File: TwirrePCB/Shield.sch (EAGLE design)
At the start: 60 parts, among them Q1 BSS138, Q2 BSS138, T3 FMMT591A, T4 FMMT491A, U1 ARDUINO-MEGAPRO

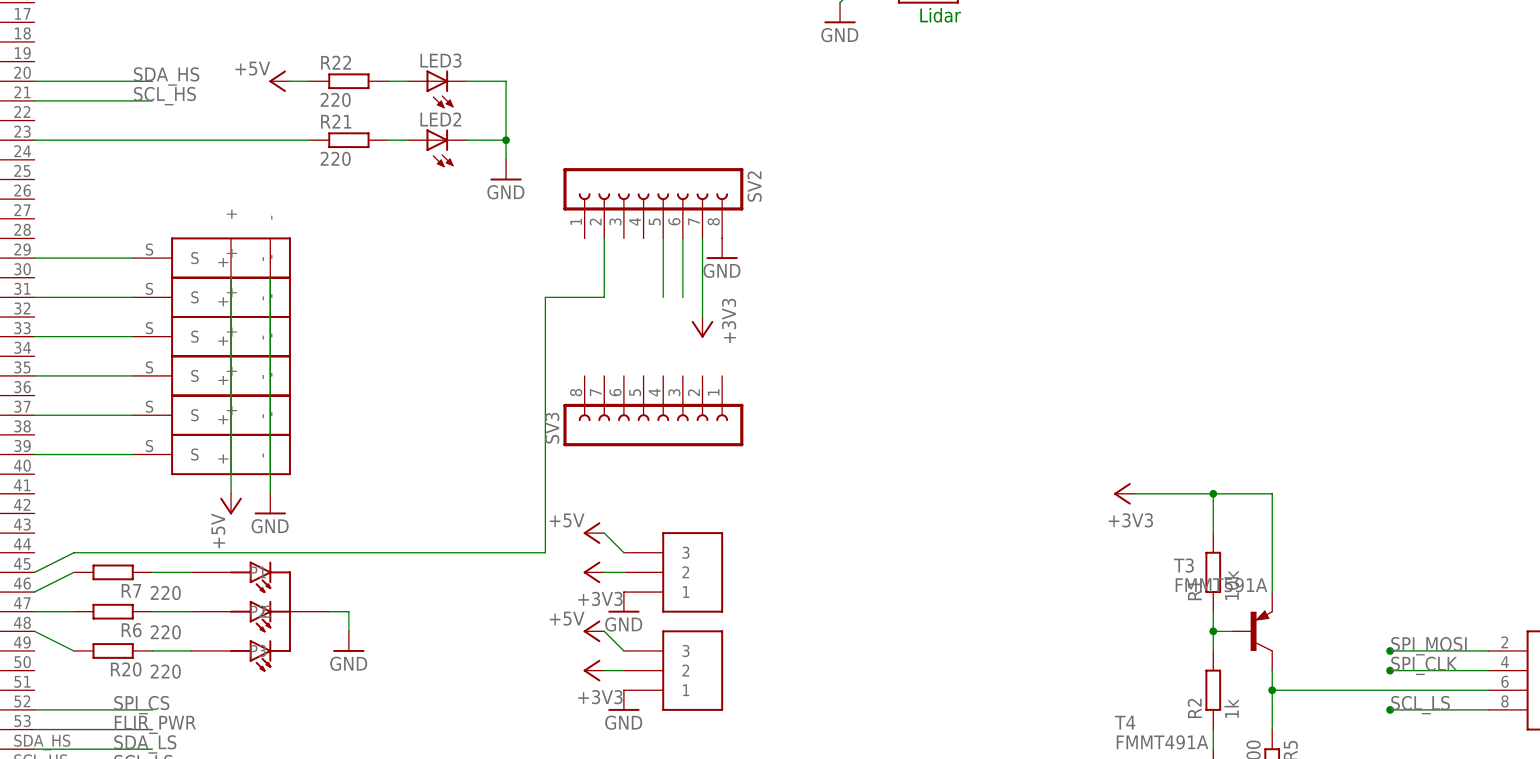
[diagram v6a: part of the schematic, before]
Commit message: Modify OLED and Servo Headers
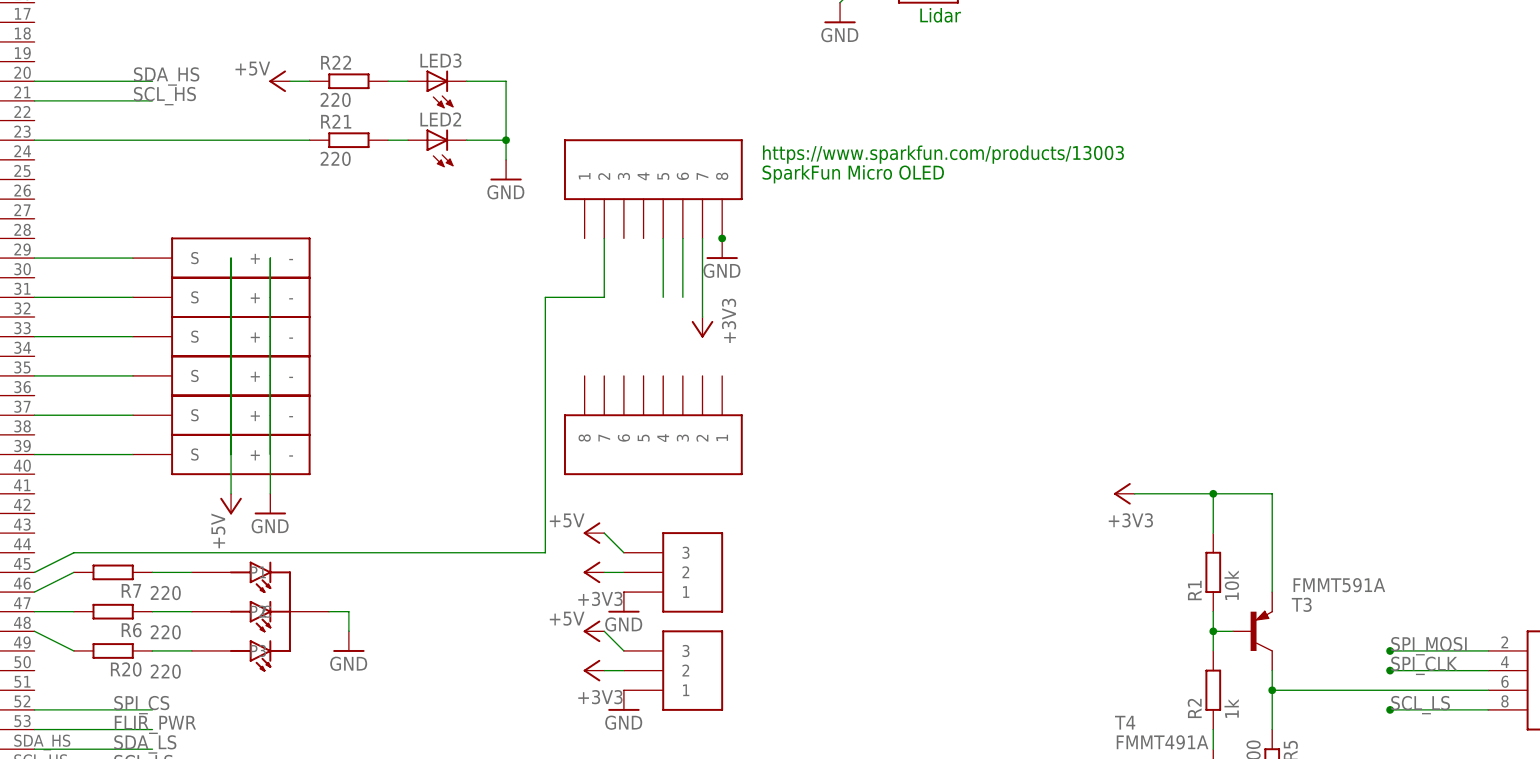
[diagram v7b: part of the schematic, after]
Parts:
- removed SV2, SV3: (no value), con-lsta:FE08-1
- added U$26, U$27: OLEDHEADER, Arduino-Boards:OLEDHEADER
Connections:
- net +3V3: now also U$26.7; no longer SV2.7
- net GND: now also U$26.8; no longer SV2.8
- net N$24: now also U$26.2; no longer SV2.2
- net SCL_LS: now also U$26.5; no longer SV2.5
- net SDA_LS: now also U$26.6; no longer SV2.6
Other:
- note added: "SparkFun Micro OLED"
- note added: "https://www.sparkfun.com/products/13003"
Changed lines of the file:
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@@
 <part name="P+5" library="supply1" deviceset="+5V" device=""/>
 <part name="U$13" library="Arduino-Boards" deviceset="JST-5" device="" value="LIDAR"/>
-<part name="SV2" library="con-lsta" deviceset="FE08-1" device=""/>
-<part name="SV3" library="con-lsta" deviceset="FE08-1" device=""/>
 <part name="GND16" library="supply1" deviceset="GND" device=""/>
 <part name="+3V7" library="supply1" deviceset="+3V3" device=""/>
@@
 <part name="T3" library="transistor" deviceset="*-PNP-" device="SOT23-BCE" value="FMMT591A "/>
 <part name="T4" library="transistor" deviceset="*-NPN-" device="SOT23-BEC" technology="BC808" value="FMMT491A "/>
+<part name="U$26" library="Arduino-Boards" deviceset="OLEDHEADER" device=""/>
+<part name="U$27" library="Arduino-Boards" deviceset="OLEDHEADER" device=""/>
 </parts>
 <sheets>
@@
 <text x="-17.78" y="53.34" size="1.778" layer="91" rot="R90">PWM IN</text>
 <text x="-17.78" y="25.4" size="1.778" layer="91" rot="R90">PWM OUT</text>
+<text x="167.64" y="99.06" size="1.778" layer="91">https://www.sparkfun.com/products/13003</text>
+<text x="167.64" y="96.52" size="1.778" layer="91">SparkFun Micro OLED</text>
 </plain>
 <instances>
@@
 </instance>
 <instance part="U$13" gate="G$1" x="-137.16" y="88.9" rot="R180"/>
-<instance part="SV2" gate="G$1" x="152.4" y="96.52" rot="R270"/>
-<instance part="SV3" gate="G$1" x="154.94" y="63.5" rot="R90"/>
 <instance part="GND16" gate="1" x="162.56" y="86.36"/>
 <instance part="+3V7" gate="G$1" x="160.02" y="76.2" rot="R180"/>
@@
 <instance part="+3V10" gate="G$1" x="55.88" y="187.96"/>
 <instance part="U$25" gate="G$1" x="274.32" y="30.48" rot="MR0"/>
-<instance part="T3" gate="G$1" x="231.14" y="38.1"/>
+<instance part="T3" gate="G$1" x="231.14" y="38.1" smashed="yes">
+<attribute name="NAME" x="236.22" y="40.64" size="1.778" layer="95"/>
+<attribute name="VALUE" x="236.22" y="43.18" size="1.778" layer="96"/>
+</instance>
 <instance part="T4" gate="G$1" x="223.52" y="17.78"/>
+<instance part="U$26" gate="G$1" x="152.4" y="88.9"/>
+<instance part="U$27" gate="G$1" x="154.94" y="71.12" rot="R180"/>
 </instances>
 <busses>
@@
 </segment>
 <segment>
-<pinref part="SV2" gate="G$1" pin="8"/>
 <pinref part="GND16" gate="1" pin="GND"/>
+<pinref part="U$26" gate="G$1" pin="8"/>
+<junction x="162.56" y="88.9"/>
+<pinref part="U$26" gate="G$1" pin="8"/>
 </segment>
 <segment>
@@
 <pinref part="U$19" gate="G$1" pin="-"/>
 <pinref part="GND17" gate="1" pin="GND"/>
-<wire x1="104.14" y1="55.88" x2="104.14" y2="58.42" width="0.1524" layer="91"/>
 <pinref part="U$24" gate="G$1" pin="-"/>
 <pinref part="U$23" gate="G$1" pin="-"/>
-<wire x1="104.14" y1="83.82" x2="104.14" y2="78.74" width="0.1524" layer="91"/>
 <pinref part="U$22" gate="G$1" pin="-"/>
-<wire x1="104.14" y1="78.74" x2="104.14" y2="73.66" width="0.1524" layer="91"/>
 <pinref part="U$21" gate="G$1" pin="-"/>
-<wire x1="104.14" y1="73.66" x2="104.14" y2="68.58" width="0.1524" layer="91"/>
 <pinref part="U$20" gate="G$1" pin="-"/>
-<wire x1="104.14" y1="68.58" x2="104.14" y2="63.5" width="0.1524" layer="91"/>
-<wire x1="104.14" y1="63.5" x2="104.14" y2="58.42" width="0.1524" layer="91"/>
+<wire x1="104.14" y1="86.36" x2="104.14" y2="55.88" width="0.1524" layer="91"/>
+<wire x1="104.14" y1="86.36" x2="104.14" y2="81.28" width="0.1524" layer="91"/>
+<wire x1="104.14" y1="81.28" x2="104.14" y2="76.2" width="0.1524" layer="91"/>
+<wire x1="104.14" y1="76.2" x2="104.14" y2="71.12" width="0.1524" layer="91"/>
+<wire x1="104.14" y1="71.12" x2="104.14" y2="66.04" width="0.1524" layer="91"/>
+<wire x1="104.14" y1="66.04" x2="104.14" y2="60.96" width="0.1524" layer="91"/>
 </segment>
 <segment>
@@
 </segment>
 <segment>
-<pinref part="SV2" gate="G$1" pin="7"/>
 <pinref part="+3V7" gate="G$1" pin="+3V3"/>
 <wire x1="160.02" y1="78.74" x2="160.02" y2="88.9" width="0.1524" layer="91"/>
+<pinref part="U$26" gate="G$1" pin="7"/>
 </segment>
 <segment>
@@
 </segment>
 <segment>
-<pinref part="SV2" gate="G$1" pin="5"/>
 <wire x1="154.94" y1="88.9" x2="154.94" y2="81.28" width="0.1524" layer="91"/>
+<pinref part="U$26" gate="G$1" pin="5"/>
 </segment>
 <segment>
@@
 </segment>
 <segment>
-<pinref part="SV2" gate="G$1" pin="6"/>
 <wire x1="157.48" y1="88.9" x2="157.48" y2="81.28" width="0.1524" layer="91"/>
+<pinref part="U$26" gate="G$1" pin="6"/>
 </segment>
 <segment>
@@
 <pinref part="U$19" gate="G$1" pin="+"/>
 <pinref part="P+6" gate="1" pin="+5V"/>
-<wire x1="99.06" y1="55.88" x2="99.06" y2="58.42" width="0.1524" layer="91"/>
 <pinref part="U$20" gate="G$1" pin="+"/>
-<wire x1="99.06" y1="58.42" x2="99.06" y2="63.5" width="0.1524" layer="91"/>
+<wire x1="99.06" y1="55.88" x2="99.06" y2="86.36" width="0.1524" layer="91"/>
 <pinref part="U$21" gate="G$1" pin="+"/>
-<wire x1="99.06" y1="63.5" x2="99.06" y2="68.58" width="0.1524" layer="91"/>
 <pinref part="U$22" gate="G$1" pin="+"/>
-<wire x1="99.06" y1="68.58" x2="99.06" y2="73.66" width="0.1524" layer="91"/>
 <pinref part="U$23" gate="G$1" pin="+"/>
-<wire x1="99.06" y1="73.66" x2="99.06" y2="78.74" width="0.1524" layer="91"/>
 <pinref part="U$24" gate="G$1" pin="+"/>
-<wire x1="99.06" y1="78.74" x2="99.06" y2="83.82" width="0.1524" layer="91"/>
+<wire x1="99.06" y1="86.36" x2="99.06" y2="81.28" width="0.1524" layer="91"/>
+<wire x1="99.06" y1="81.28" x2="99.06" y2="76.2" width="0.1524" layer="91"/>
+<wire x1="99.06" y1="76.2" x2="99.06" y2="71.12" width="0.1524" layer="91"/>
+<wire x1="99.06" y1="71.12" x2="99.06" y2="66.04" width="0.1524" layer="91"/>
+<wire x1="99.06" y1="66.04" x2="99.06" y2="60.96" width="0.1524" layer="91"/>
 </segment>
 <segment>
@@
 <net name="N$24" class="0">
 <segment>
-<pinref part="SV2" gate="G$1" pin="2"/>
 <wire x1="147.32" y1="88.9" x2="147.32" y2="81.28" width="0.1524" layer="91"/>
 <wire x1="147.32" y1="81.28" x2="139.7" y2="81.28" width="0.1524" layer="91"/>
@@
 <pinref part="U1" gate="G$1" pin="45"/>
 <wire x1="78.74" y1="48.26" x2="73.66" y2="45.72" width="0.1524" layer="91"/>
-</segment>
-</net>
+<pinref part="U$26" gate="G$1" pin="2"/>
+</segment>
+</net>

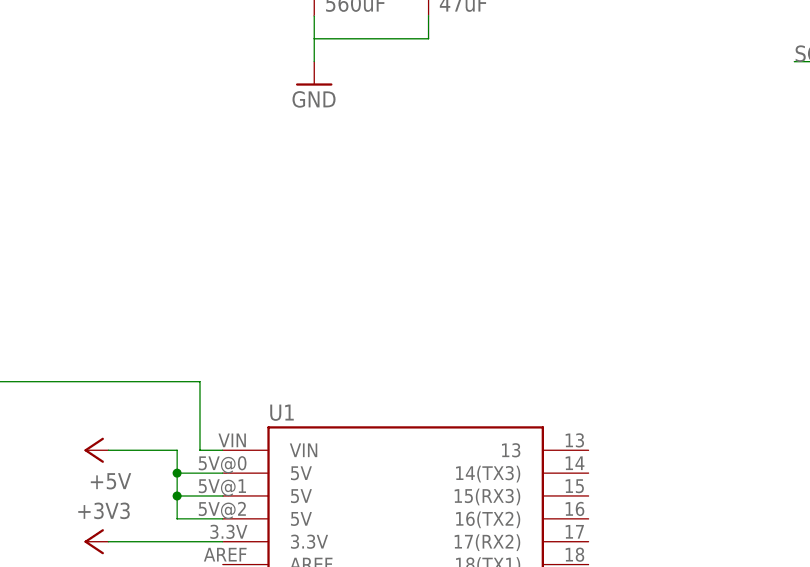
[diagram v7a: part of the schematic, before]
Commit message: Add NHL Computer Vision Logo
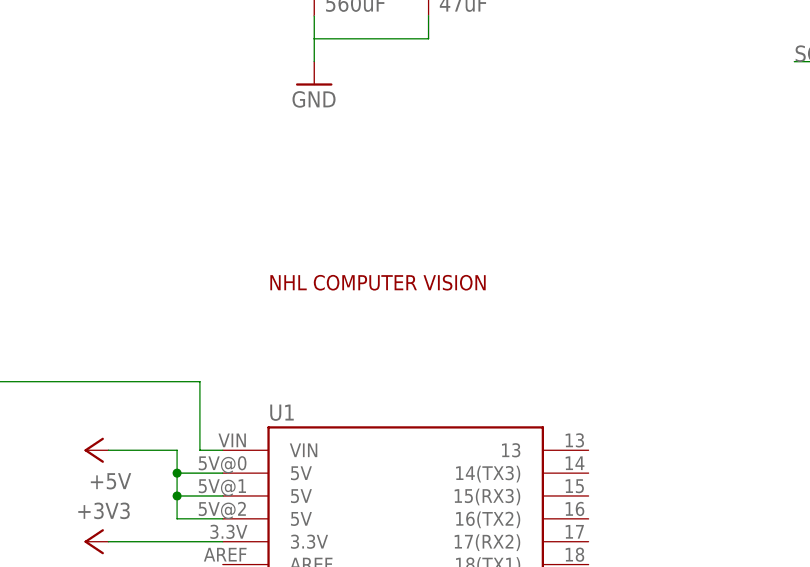
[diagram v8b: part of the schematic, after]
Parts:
- added U$28: NHLLOGO, Arduino-Boards:NHLLOGO
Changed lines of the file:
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@@
 <part name="U$26" library="Arduino-Boards" deviceset="OLEDHEADER" device=""/>
 <part name="U$27" library="Arduino-Boards" deviceset="OLEDHEADER" device=""/>
+<part name="U$28" library="Arduino-Boards" deviceset="NHLLOGO" device=""/>
 </parts>
 <sheets>
@@
 <instance part="U$26" gate="G$1" x="152.4" y="88.9"/>
 <instance part="U$27" gate="G$1" x="154.94" y="71.12" rot="R180"/>
+<instance part="U$28" gate="G$1" x="50.8" y="144.78"/>
 </instances>
 <busses>
